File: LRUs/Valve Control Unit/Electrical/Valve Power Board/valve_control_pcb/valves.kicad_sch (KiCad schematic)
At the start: 6 parts

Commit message: Commit valve board updates
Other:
- sheet Valve 1 ports: added KELVIN_SENSE; removed none
- sheet Valve 2 ports: added KELVIN_SENSE; removed none
- sheet Valve 3 ports: added KELVIN_SENSE; removed none
- sheet Valve 4 ports: added KELVIN_SENSE; removed none
- sheet Valve 5 ports: added KELVIN_SENSE; removed none
- sheet Valve 6 ports: added KELVIN_SENSE; removed none
- note added: "VALVES"
- title: (none) -> VALVES

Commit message: Committttt
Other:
- sheet Valve 1 ports: added VSENSE_N, VSENSE_P; removed KELVIN_SENSE
- sheet Valve 2 ports: added VSENSE_N, VSENSE_P; removed KELVIN_SENSE
- sheet Valve 3 ports: added VSENSE_N, VSENSE_P; removed KELVIN_SENSE
- sheet Valve 4 ports: added VSENSE_N, VSENSE_P; removed KELVIN_SENSE
- sheet Valve 5 ports: added VSENSE_N, VSENSE_P; removed KELVIN_SENSE
- sheet Valve 6 ports: added VSENSE_N, VSENSE_P; removed KELVIN_SENSE

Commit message: Commit da changes
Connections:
- net Valve 1/VIN renamed 12V_VALVES
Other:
- added sheet Gate Drivers (gate_driver.kicad_sch)
- note added: "19"
- note added: "20"
- note added: "32"
- moved on the sheet: C67, C68, C69, C70, C71, C72

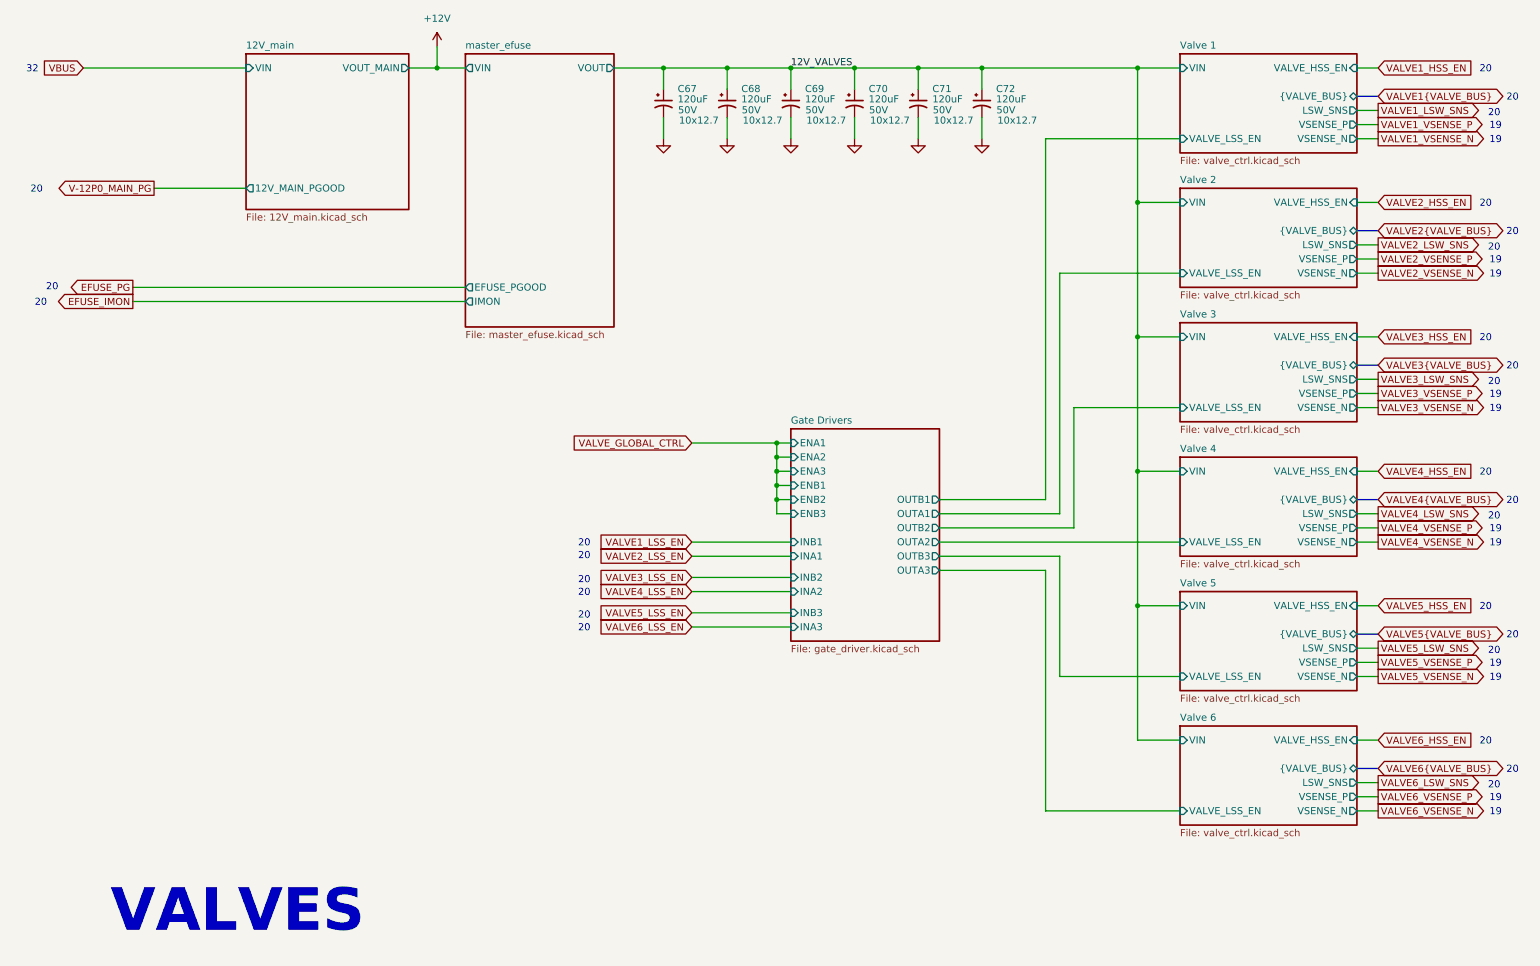
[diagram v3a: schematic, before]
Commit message: Major changes due to architecture
Added battery muxing for valve power, igniter system, and separate system battery for control electronics
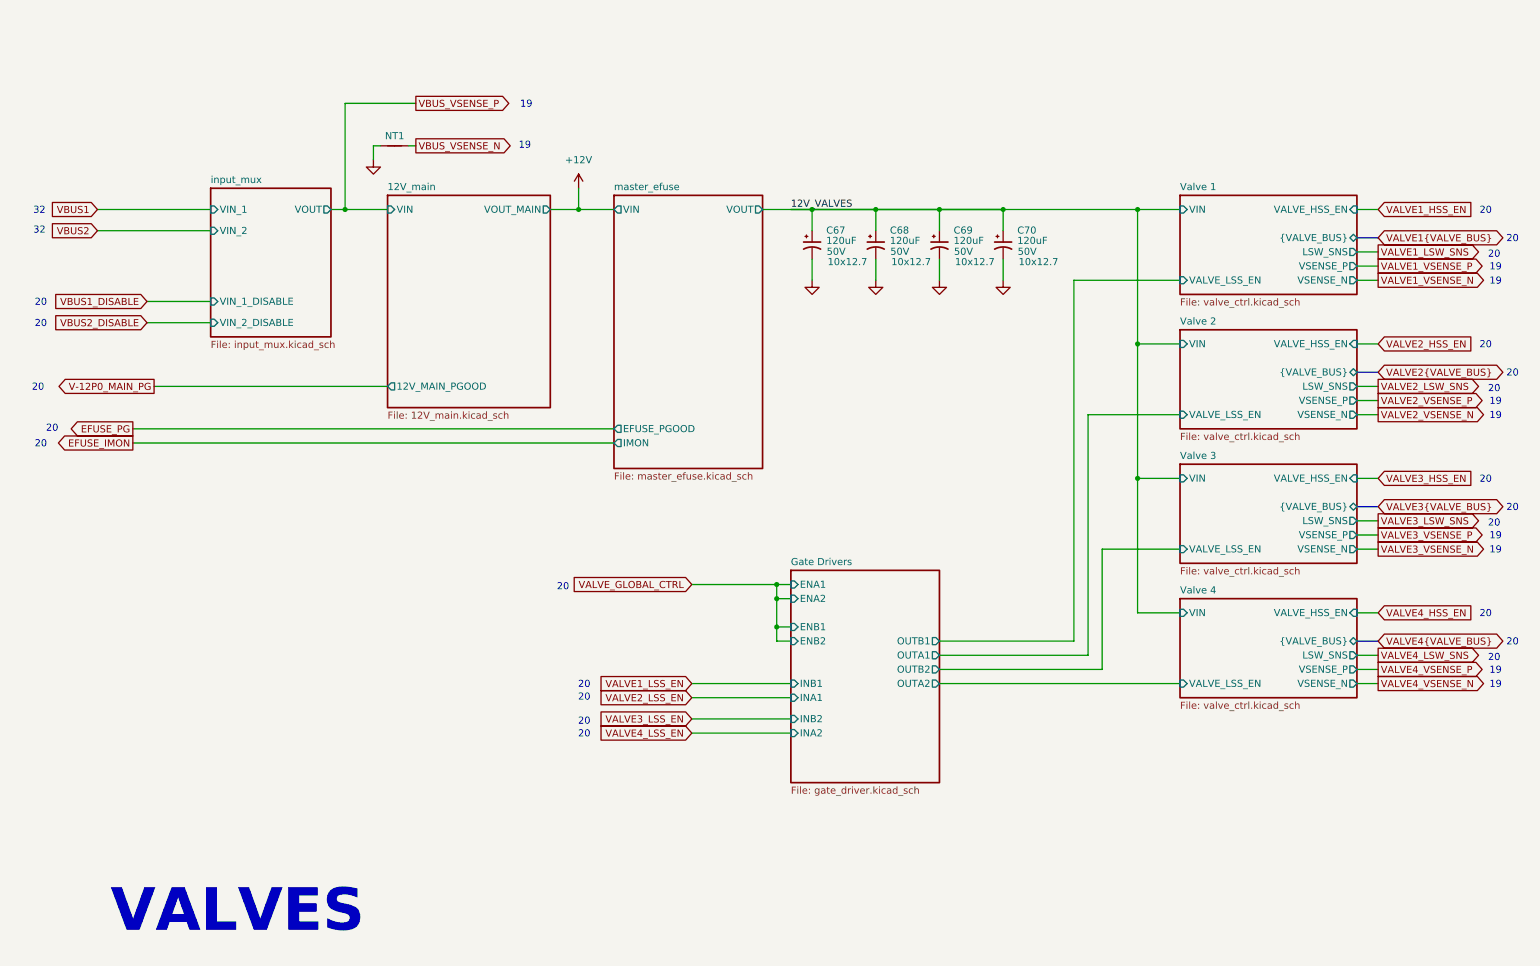
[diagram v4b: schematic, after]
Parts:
- removed C71, C72: 120uF, Capacitor_SMD:CP_Elec_10x12.6, symbol Device:C_Polarized_Small_US
- added NT1: NetTie_2, NetTie:NetTie-2_SMD_Pad0.5mm, symbol Device:NetTie_2
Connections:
- net GND: now also NT1.1
- new net VBUS_VSENSE_N: NT1.2
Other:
- removed sheet Valve 5
- removed sheet Valve 6
- added sheet input_mux (input_mux.kicad_sch)
- sheet Gate Drivers ports: added none; removed ENA3, ENB3, INA3, INB3, OUTA3, OUTB3
- moved on the sheet: C67, C68, C69, C70

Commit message: Fixes
Added hops, fixed the planes, and fixed minor issues
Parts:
- renumbered C67 to C13, C68 to C14, C69 to C15, C70 to C16
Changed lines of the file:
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@@
 		(in_pos_files yes)
 		(dnp no)
-		(property "Reference" "C68"
+		(property "Reference" "C14"
 			(at 170.18 54.5339 0)
 			(show_name no)
@@
 			(project "valve_control_pcb"
 				(path "/d4e8203a-d76f-4c3b-b909-1a52c35190e7"
-					(reference "C68")
+					(reference "C14")
 					(unit 1)
 				)
@@
 		(dnp no)
 		(fields_autoplaced yes)
-		(property "Reference" "#PWR0373"
+		(property "Reference" "#PWR031"
 			(at 114.3 50.8 0)
 			(hide yes)
@@
 			(project "valve_control_pcb"
 				(path "/d4e8203a-d76f-4c3b-b909-1a52c35190e7"
-					(reference "#PWR0373")
+					(reference "#PWR031")
 					(unit 1)
 				)
@@
 		(dnp no)
 		(fields_autoplaced yes)
-		(property "Reference" "#PWR0180"
+		(property "Reference" "#PWR033"
 			(at 167.64 69.85 0)
 			(hide yes)
@@
 			(project "valve_control_pcb"
 				(path "/d4e8203a-d76f-4c3b-b909-1a52c35190e7"
-					(reference "#PWR0180")
+					(reference "#PWR033")
 					(unit 1)
 				)
@@
 		(in_pos_files yes)
 		(dnp no)
-		(property "Reference" "C69"
+		(property "Reference" "C15"
 			(at 181.61 54.5339 0)
 			(show_name no)
@@
 			(project "valve_control_pcb"
 				(path "/d4e8203a-d76f-4c3b-b909-1a52c35190e7"
-					(reference "C69")
+					(reference "C15")
 					(unit 1)
 				)
@@
 		(in_pos_files yes)
 		(dnp no)
-		(property "Reference" "C67"
+		(property "Reference" "C13"
 			(at 158.75 54.5339 0)
 			(show_name no)
@@
 			(project "valve_control_pcb"
 				(path "/d4e8203a-d76f-4c3b-b909-1a52c35190e7"
-					(reference "C67")
+					(reference "C13")
 					(unit 1)
 				)
@@
 		(dnp no)
 		(fields_autoplaced yes)
-		(property "Reference" "#PWR0182"
+		(property "Reference" "#PWR035"
 			(at 190.5 69.85 0)
 			(hide yes)
@@
 			(project "valve_control_pcb"
 				(path "/d4e8203a-d76f-4c3b-b909-1a52c35190e7"
-					(reference "#PWR0182")
+					(reference "#PWR035")
 					(unit 1)
 				)
@@
 		(dnp no)
 		(fields_autoplaced yes)
-		(property "Reference" "#PWR0179"
+		(property "Reference" "#PWR032"
 			(at 156.21 69.85 0)
 			(hide yes)
@@
 			(project "valve_control_pcb"
 				(path "/d4e8203a-d76f-4c3b-b909-1a52c35190e7"
-					(reference "#PWR0179")
+					(reference "#PWR032")
 					(unit 1)
 				)
@@
 		(in_pos_files yes)
 		(dnp no)
-		(property "Reference" "C70"
+		(property "Reference" "C16"
 			(at 193.04 54.5339 0)
 			(show_name no)
@@
 			(project "valve_control_pcb"
 				(path "/d4e8203a-d76f-4c3b-b909-1a52c35190e7"
-					(reference "C70")
+					(reference "C16")
 					(unit 1)
 				)
@@
 		(dnp no)
 		(fields_autoplaced yes)
-		(property "Reference" "#PWR0359"
+		(property "Reference" "#PWR030"
 			(at 77.47 48.26 0)
 			(hide yes)
@@
 			(project "valve_control_pcb"
 				(path "/d4e8203a-d76f-4c3b-b909-1a52c35190e7"
-					(reference "#PWR0359")
+					(reference "#PWR030")
 					(unit 1)
 				)
@@
 		(dnp no)
 		(fields_autoplaced yes)
-		(property "Reference" "#PWR0181"
+		(property "Reference" "#PWR034"
 			(at 179.07 69.85 0)
 			(hide yes)
@@
 			(project "valve_control_pcb"
 				(path "/d4e8203a-d76f-4c3b-b909-1a52c35190e7"
-					(reference "#PWR0181")
-					(unit 1)
-				)
+					(reference "#PWR034")
+					(unit 1)
+				)
